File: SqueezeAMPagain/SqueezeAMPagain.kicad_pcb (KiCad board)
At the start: 2 copper layers, 100 x 100 mm, 197 parts, among them J1 Conn_01x02_Pin, J10 Conn_02x07_Odd_Even, J2 Conn_01x02_Pin, J3 Conn_01x06_Pin, J4 Raspberry_Pi_2_3, J5 Conn_02x10_Odd_Even, J6 Barrel_Jack_Switch, J7 Conn_01x02_Pin, J8 USB_B_Micro, J9 Conn_01x06_Pin, Q1 Q_NPN_BEC, Q10 AO3401A, Q11 Q_NPN_BEC, Q2 AO3401A, Q3 AO3401A, Q4 AO3401A, Q5 Q_NPN_BEC, Q6 AO3401A, Q7 AO3401A, Q8 Q_NPN_BEC, Q9 Q_NPN_BEC, U1 TAS5756M, U2 ESP32-WROVER-E, U3 RaspberryPi_Pico_W, U4 TSOP21xx, U5 AMS1117-3.3, U6 TPS5430DDA, U7 CP2102N-Axx-xQFN28

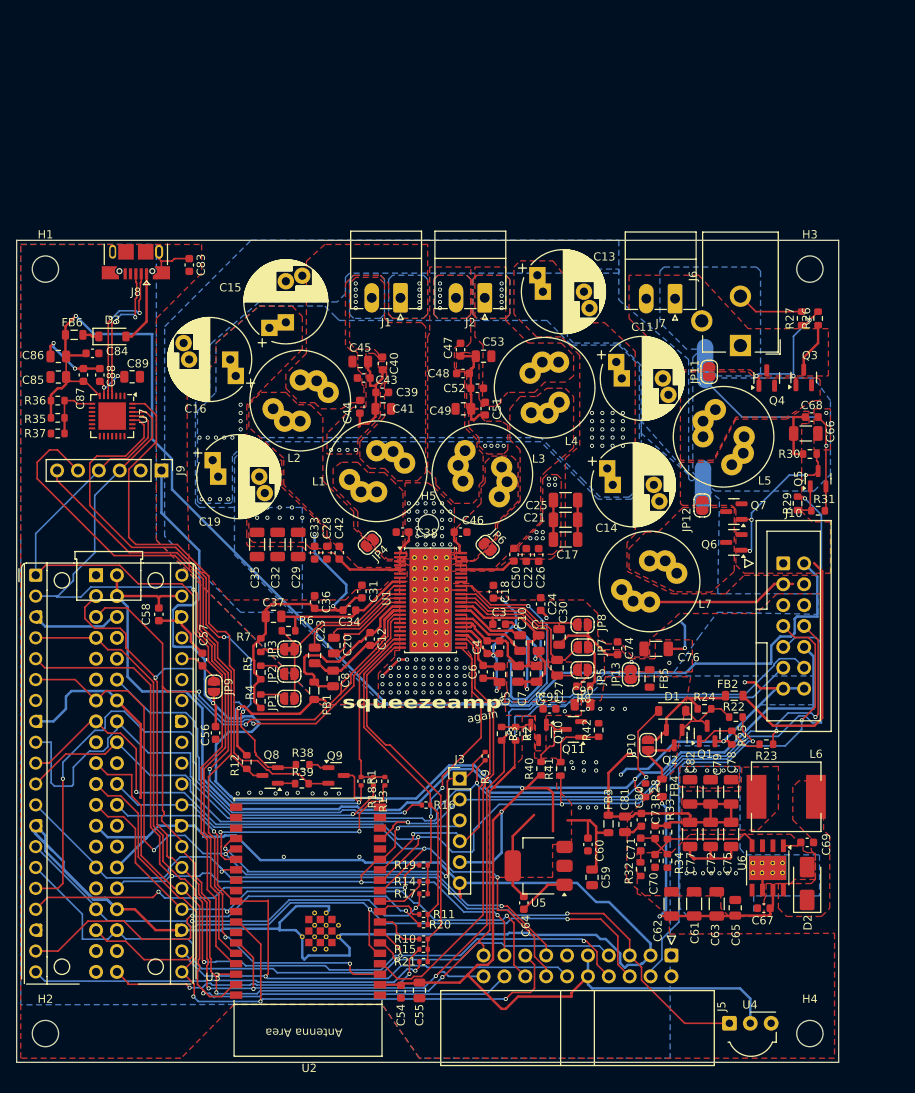
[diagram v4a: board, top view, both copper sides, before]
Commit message: Update SqueezeAMPagain.kicad_pcb, SqueezeAMPagain.kicad_prl, SqueezeAMPagain.kicad_pro, and 5 more files
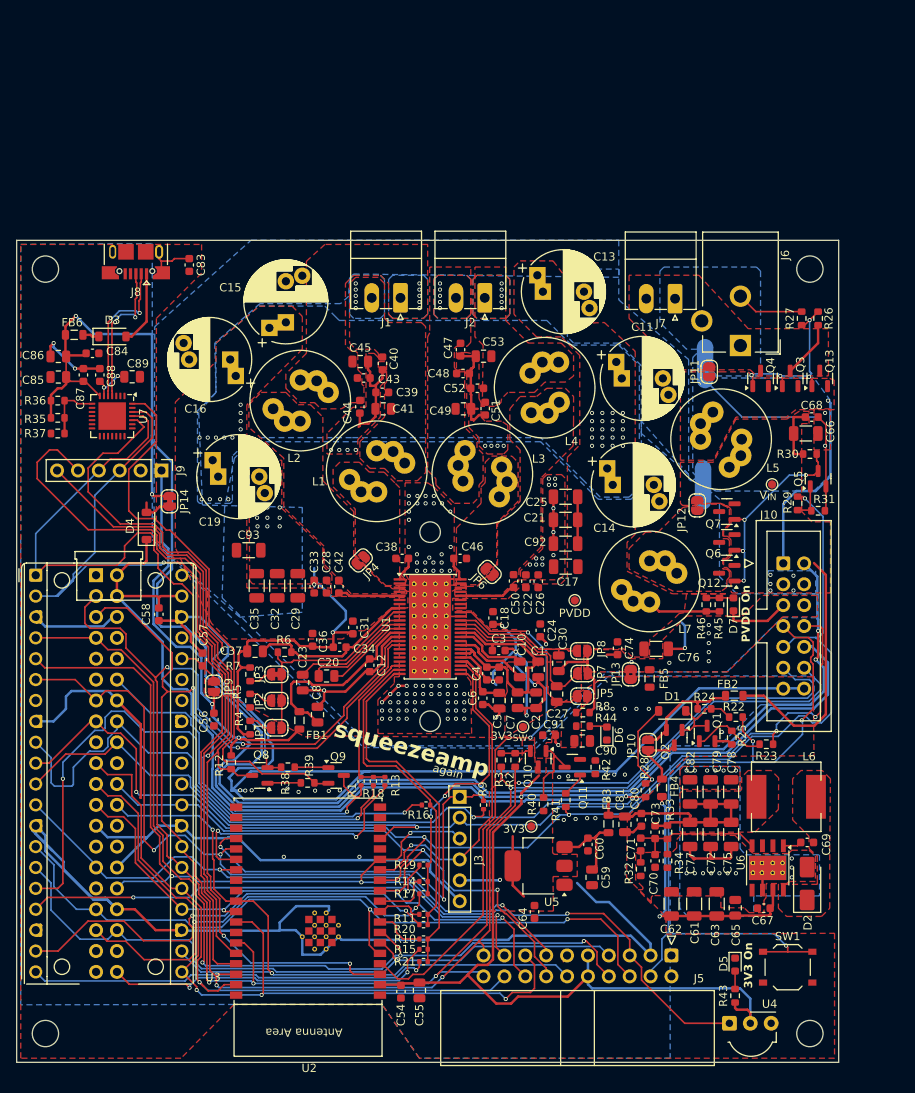
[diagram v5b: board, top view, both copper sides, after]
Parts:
- added C92: 10u/50V, Capacitor_SMD:C_1206_3216Metric, F.Cu at (124.8, 82.4)
- added C93: 10u/50V, Capacitor_SMD:C_1206_3216Metric, F.Cu at (86.2, 83.2)
- added D4: B5819W, Diode_SMD:D_SOD-123, F.Cu at (73.8, 80.2)
- added D5: LED, LED_SMD:LED_0603_1608Metric, F.Cu at (145.4, 133.6)
- added D6: LED, LED_SMD:LED_0603_1608Metric, F.Cu at (129.8, 105.5)
- added D7: LED, LED_SMD:LED_0603_1608Metric, F.Cu at (145.2, 89.8)
- added H6: MountingHole, MountingHole:MountingHole_2.5mm, F.Cu at (108.3, 104.0)
- added JP14: SolderJumper_2_Bridged, Jumper:SolderJumper-2_P1.3mm_Bridged_RoundedPad1.0x1.5mm, F.Cu at (76.6, 77.2)
- added Q12: AO3401A, Package_TO_SOT_SMD:SOT-23, F.Cu at (144.4, 86.0)
- added Q13: AO3401A, Package_TO_SOT_SMD:SOT-23, F.Cu at (155.7, 62.3)
- added R43: 330, Resistor_SMD:R_0603_1608Metric, F.Cu at (145.4, 137.4)
- added R44: 330, Resistor_SMD:R_0603_1608Metric, F.Cu at (126.9, 104.6)
- added R45: 10k, Resistor_SMD:R_0603_1608Metric, F.Cu at (143.5, 89.8)
- added R46: 10k, Resistor_SMD:R_0603_1608Metric, F.Cu at (141.9, 89.8)
- added SW1: SW_MEC_5E, Button_Switch_SMD:SW_Push_1P1T_XKB_TS-1187A, F.Cu at (151.8, 133.9)
- added TP1: 3V3, TestPoint:TestPoint_Pad_D1.0mm, F.Cu at (120.6, 116.8)
- added TP2: 3V3_{SW}, TestPoint:TestPoint_Pad_D1.0mm, F.Cu at (119.6, 104.7)
- added TP3: PVDD, TestPoint:TestPoint_Pad_D1.0mm, F.Cu at (125.9, 89.3)
- added TP4: V_{IN}, TestPoint:TestPoint_Pad_D1.0mm, F.Cu at (149.9, 75.2)
- moved R9 5.95 mm to (114.8, 114.2)
- moved C29 5.03 mm to (92.2, 87.5)
- moved C32 5.03 mm to (89.7, 87.5)
- moved C35 5.03 mm to (87.2, 87.5)
- moved C37 4.81 mm to (87.0, 95.5)
- moved C8 4.79 mm to (94.6, 103.2)
- moved C34 4.65 mm to (97.3, 95.0)
- moved C36 4.61 mm to (94.0, 94.1)
- moved Q11 4.60 mm to (125.6, 109.6)
- moved R42 4.54 mm to (128.4, 109.6)
- moved C31 4.51 mm to (98.9, 92.6)
- moved C90 4.40 mm to (126.8, 106.4)
- moved R40 4.34 mm to (122.1, 114.1)
- moved C28 4.13 mm to (95.7, 87.6)
- moved C33 4.13 mm to (94.2, 87.6)
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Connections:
- J10 pad 1: V_{IN} -> V_{supply}
- J10 pad 3: PVDD -> V_{IN}
- J10 pad 4: PVDD -> V_{IN}
- J8 pad 6nc1: Net-(J8-Shield) -> (no net)
- J8 pad 6nc2: Net-(J8-Shield) -> (no net)
- JP11 pad 2: /Power/V_{supply} -> V_{supply}
- L5 pad 1: /Power/V_{supply} -> V_{supply}
- Q3 pad 2: /Power/V_{supply} -> V_{supply}
- Q4 pad 2: /Power/V_{supply} -> V_{supply}
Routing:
- net GND: track 310.2 -> 381.0 mm, vias 43 -> 45
- net V_{USB}: track 154.3 -> 206.1 mm, vias 1 -> 4
- net +3.3V: track 291.9 -> 258.6 mm, vias 6 -> 5
- net V_{supply}: track 0.00 -> 23.7 mm, vias 0 -> 1
- net /FPConnector/~{WAKE}: track 63.6 -> 87.3 mm, vias 2 -> 3
- net +3.3V_{SW}: track 45.1 -> 30.8 mm
- net PVDD: track 23.2 -> 14.0 mm
- net /USB-Uart/RX: track 98.2 -> 105.2 mm
- net PGND: track 161.2 -> 167.6 mm
- net Net-(Q12-G): track 19.4 -> 24.6 mm, vias 3 -> 4
- net Net-(Q8-E): track 67.4 -> 62.3 mm
- net +5V: track 135.4 -> 130.8 mm, vias 2 -> 1
- net Net-(D4-A): track 0.00 -> 4.29 mm
- net Net-(Q11-B): track 7.19 -> 2.94 mm
- net /Amp/~{SPK_FAULT}: track 69.5 -> 65.5 mm
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- added copper zone on B.Cu, net V_{IN}
- added copper zone on F.Cu, net V_{supply}
- removed copper zone on F.Cu, net /Power/V_{supply}
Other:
- board text added: "${REFERENCE}"
- board text added: "3V3 On"
- board text added: "PVDD On"

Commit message: Update SqueezeAMPagain.kicad_pcb, SqueezeAMPagain.kicad_prl, project.db, and 1 more file
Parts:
- L6: footprint Inductor:L_Vishay_IHLP-3232 -> Inductor_SMD:L_Chilisin_BMRB00060612
